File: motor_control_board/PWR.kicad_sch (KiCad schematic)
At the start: 16 parts

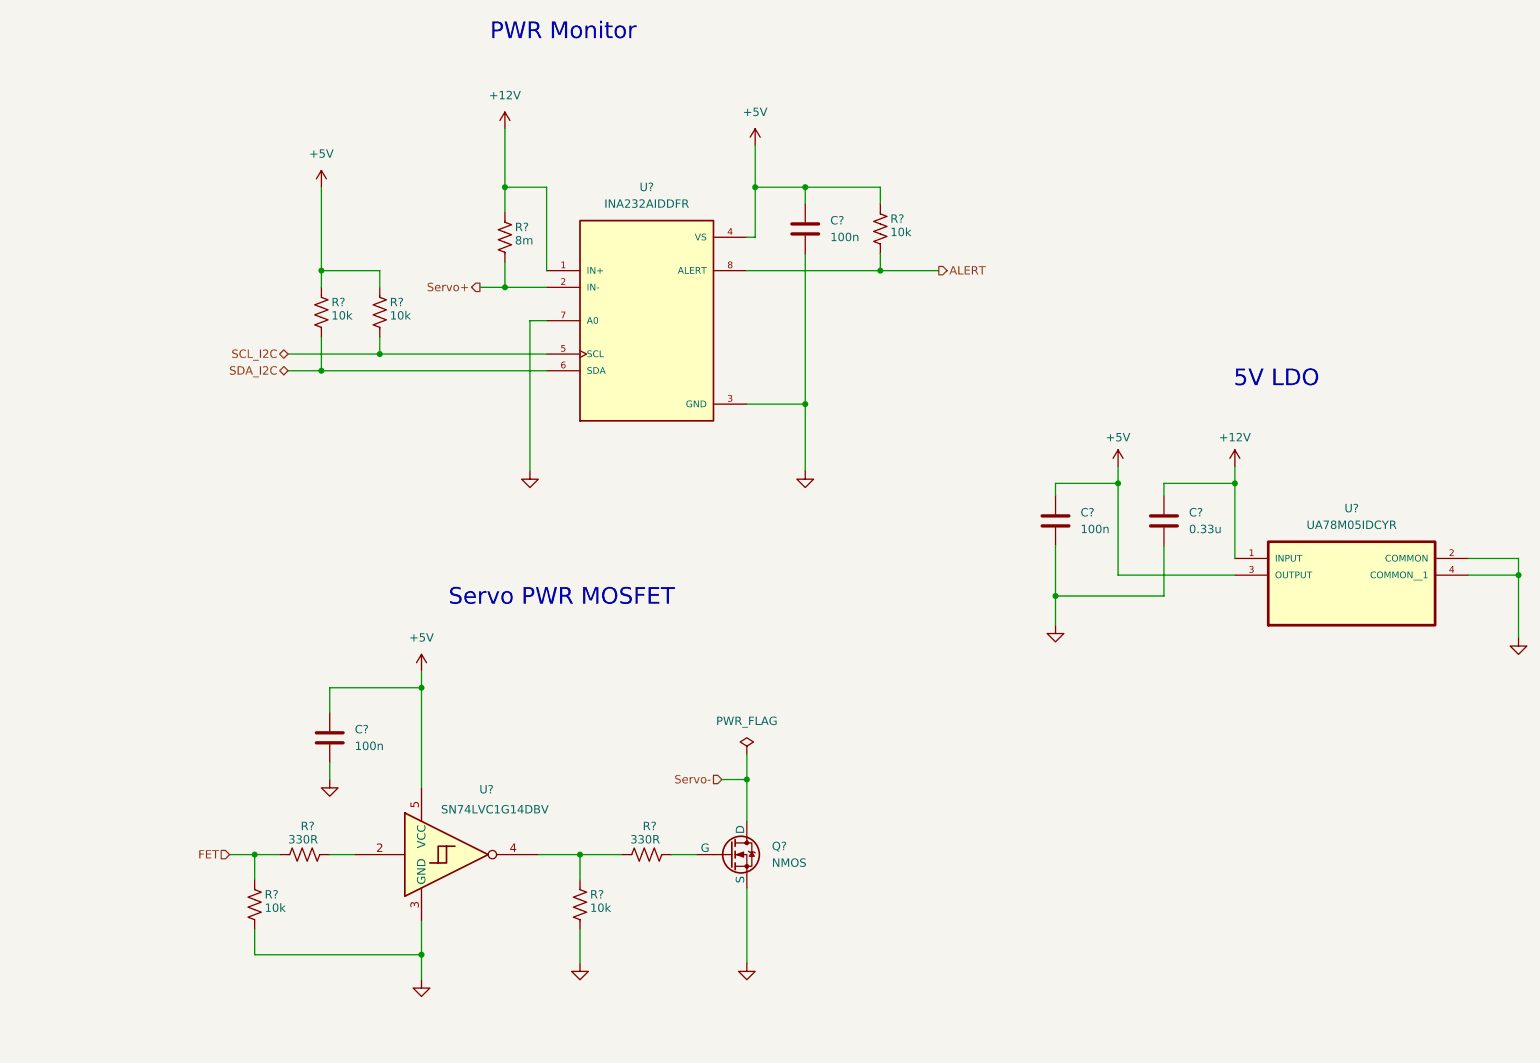
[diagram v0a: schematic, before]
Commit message: Minor schematic edits
Annotated schematic, selected mosfet and diodes, addressed comments
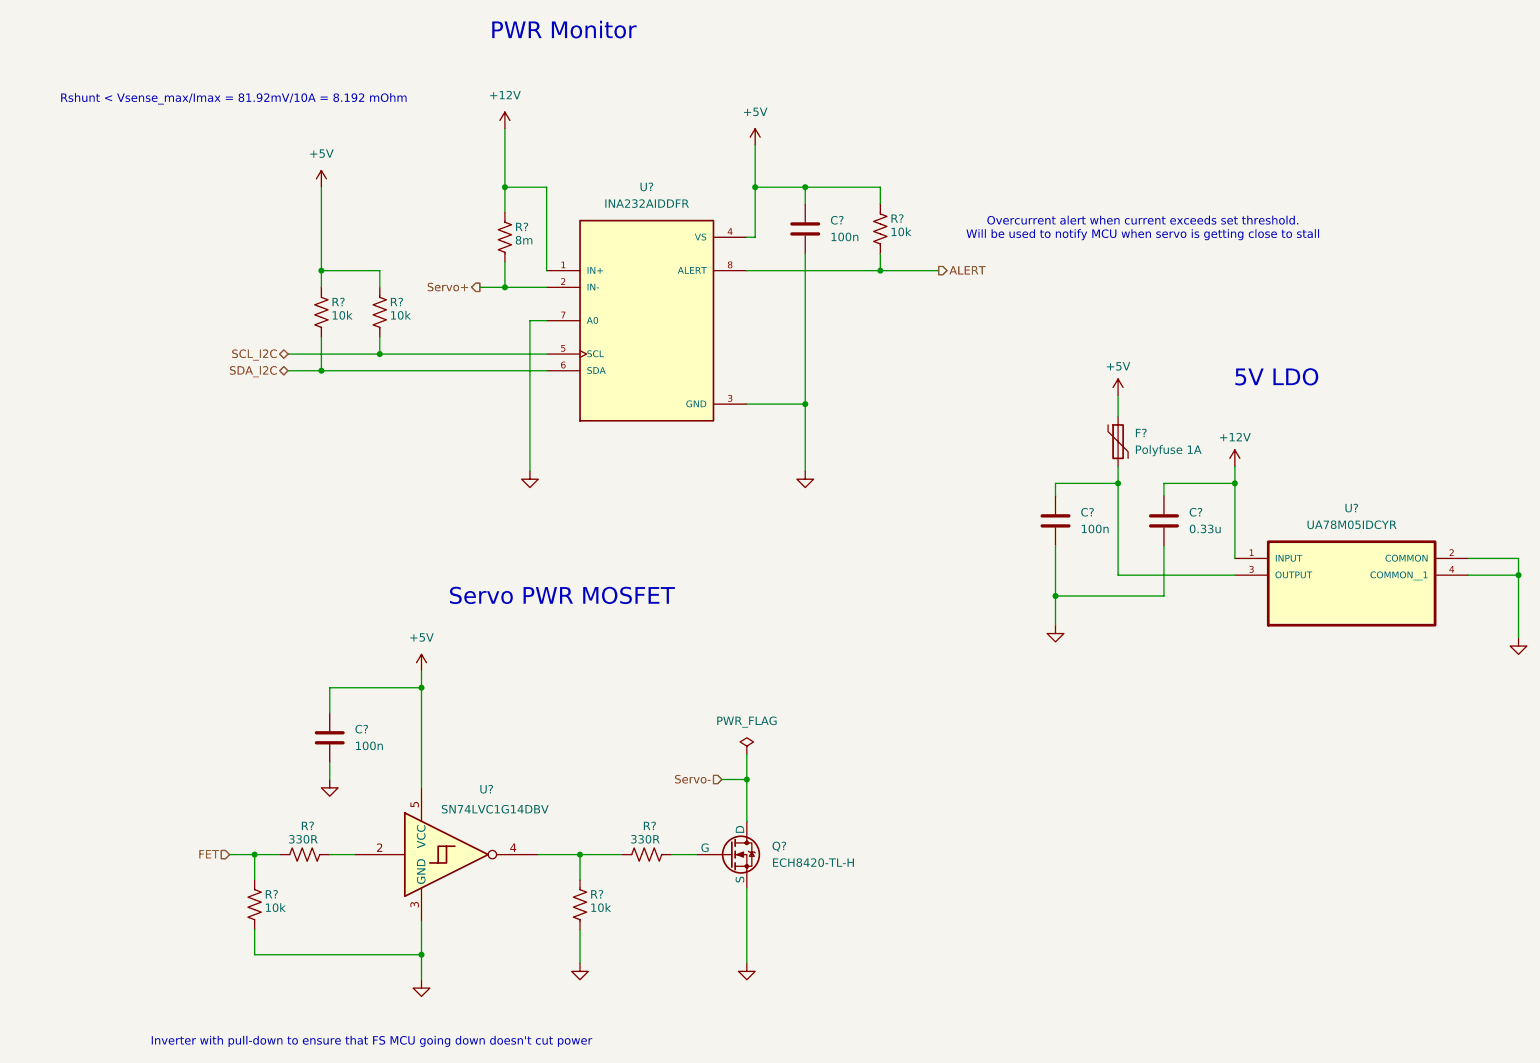
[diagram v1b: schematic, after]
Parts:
- added F?: Polyfuse 1A, symbol canhw:Polyfuse
- Q?: value NMOS -> ECH8420-TL-H
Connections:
- net +5V: now also F?.1; no longer C?.1, U?.3 (OUTPUT)
- new net: C?.1, F?.2, U?.3 (OUTPUT)
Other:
- note added: "Inverter with pull-down to ensure that FS MCU going down doesn't cut power"
- note added: "Overcurrent alert when current exceeds set threshold. Will be used to notify MCU when servo is getting close to stall"
- note added: "Rshunt < Vsense_max/Imax = 81.92mV/10A = 8.192 mOhm"
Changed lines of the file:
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@@
+	(wire
+		(pts
+			(xy 200.025 87.63) (xy 200.025 90.805)
+		)
+		(stroke
+			(width 0)
+			(type default)
+		)
+	)
 	(wire
 		(pts
@@
 		)
 	)
+	(text "Inverter with pull-down to ensure that FS MCU going down doesn't cut power"
+		(exclude_from_sim no)
+		(at 86.36 186.055 0)
+		(effects
+			(font
+				(size 1.27 1.27)
+			)
+		)
+	)
 	(text "5V LDO"
 		(exclude_from_sim no)
@@
 		)
 	)
+	(text "Overcurrent alert when current exceeds set threshold.\nWill be used to notify MCU when servo is getting close to stall"
+		(exclude_from_sim no)
+		(at 203.835 62.23 0)
+		(effects
+			(font
+				(size 1.27 1.27)
+			)
+		)
+	)
+	(text "Rshunt < Vsense_max/Imax = 81.92mV/10A = 8.192 mOhm"
+		(exclude_from_sim no)
+		(at 65.405 42.545 0)
+		(effects
+			(font
+				(size 1.27 1.27)
+			)
+		)
+	)
 	(hierarchical_label "SCL_I2C"
 		(shape bidirectional)
@@
 	(symbol
 		(lib_id "canhw:+5V")
-		(at 200.025 98.425 0)
+		(at 200.025 87.63 0)
 		(unit 1)
 		(exclude_from_sim no)
@@
 		(fields_autoplaced yes)
 		(property "Reference" "#PWR028"
-			(at 200.025 102.235 0)
+			(at 200.025 91.44 0)
 			(effects
 				(font
@@
 		)
 		(property "Value" "+5V"
-			(at 200.025 93.98 0)
+			(at 200.025 83.185 0)
 			(effects
 				(font
@@
 		)
 		(property "Footprint" ""
-			(at 200.025 98.425 0)
+			(at 200.025 87.63 0)
 			(effects
 				(font
@@
 		)
 		(property "Datasheet" ""
-			(at 200.025 98.425 0)
+			(at 200.025 87.63 0)
 			(effects
 				(font
@@
 		)
 		(property "Description" "Power symbol creates a global label with name \"+5V\""
-			(at 200.025 98.425 0)
+			(at 200.025 87.63 0)
 			(effects
 				(font
@@
 			)
 		)
-		(property "Value" "NMOS"
+		(property "Value" "ECH8420-TL-H"
 			(at 147.32 158.7499 0)
 			(effects
@@
 			)
 		)
-		(property "Datasheet" "https://ngspice.sourceforge.io/docs/ngspice-html-manual/manual.xhtml#cha_MOSFETs"
+		(property "Datasheet" "https://www.onsemi.com/download/data-sheet/pdf/ech8420-d.pdf"
 			(at 140.97 170.18 0)
 			(effects
@@
 			)
 		)
+		(property "Purpose" ""
+			(at 140.97 157.48 0)
+			(effects
+				(font
+					(size 1.27 1.27)
+				)
+			)
+		)
 		(pin "2"
 		)
@@
 					(unit 1)
 				)
+			)
+		)
+	)
+	(symbol
+		(lib_id "canhw:Polyfuse")
+		(at 200.025 94.615 0)
+		(unit 1)
+		(exclude_from_sim no)
+		(in_bom yes)
+		(on_board yes)
+		(dnp no)
+		(property "Reference" "F?"
+			(at 202.565 93.345 0)
+			(effects
+				(font
+					(size 1.27 1.27)
+				)
+				(justify left)
+			)
+		)
+		(property "Value" "Polyfuse 1A"
+			(at 202.565 95.885 0)
+			(effects
+				(font
+					(size 1.27 1.27)
+				)
+				(justify left)
+			)
+		)
+		(property "Footprint" ""
+			(at 201.295 99.695 0)
+			(effects
+				(font
+					(size 1.27 1.27)
+				)
+				(justify left)
+				(hide yes)
+			)
+		)
+		(property "Datasheet" "~"
+			(at 200.025 94.615 0)
+			(effects
+				(font
+					(size 1.27 1.27)
+				)
+				(hide yes)
+			)
+		)
+		(property "Description" "Resettable fuse, polymeric positive temperature coefficient"
+			(at 200.025 94.615 0)
+			(effects
+				(font
+					(size 1.27 1.27)
+				)
+				(hide yes)
+			)
+		)
+		(pin "2"
+		)
+		(pin "1"
+		)
+		(instances
+			(project "motor_control_board"
+				(path "/ced26b11-410b-4897-bfe1-68b095b3fef4/6d921c46-a69c-4b88-8fde-0dba583b7bde"
+					(reference "F?")
+					(unit 1)
+				)

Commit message: Added second encoder connection, minor edits
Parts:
- R22: renamed from R?; value 8m -> 13m
- gave numbers to parts that had none: 16
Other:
- note added: "Rshunt < Vsense_max/Imax = 81.92mV/5A = 16.384 mOhm"
- note removed: "Rshunt < Vsense_max/Imax = 81.92mV/10A = 8.192 mOhm"
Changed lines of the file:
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@@
 	)
 	(junction
-		(at 190.5 118.11)
-		(diameter 0)
-		(color 0 0 0 0)
-	)
-	(junction
 		(at 78.74 68.58)
 		(diameter 0)
@@
 	(wire
 		(pts
-			(xy 190.5 110.49) (xy 190.5 118.11)
-		)
-		(stroke
-			(width 0)
-			(type default)
-		)
-	)
-	(wire
-		(pts
 			(xy 152.4 55.88) (xy 144.78 55.88)
 		)
@@
 	(wire
 		(pts
-			(xy 190.5 118.11) (xy 190.5 122.555)
+			(xy 190.5 110.49) (xy 190.5 118.11)
 		)
 		(stroke
@@
 	(wire
 		(pts
-			(xy 207.01 118.11) (xy 190.5 118.11)
-		)
-		(stroke
-			(width 0)
-			(type default)
-		)
-	)
-	(wire
-		(pts
 			(xy 87.63 78.74) (xy 87.63 81.28)
 		)
@@
 		)
 	)
-	(text "Rshunt < Vsense_max/Imax = 81.92mV/10A = 8.192 mOhm"
+	(text "Rshunt < Vsense_max/Imax = 81.92mV/5A = 16.384 mOhm"
 		(exclude_from_sim no)
 		(at 65.405 42.545 0)
@@
 		(dnp no)
 		(fields_autoplaced yes)
-		(property "Reference" "C?"
+		(property "Reference" "C13"
 			(at 156.21 60.9599 0)
 			(effects
@@
 			(project "Motor Control Board"
 				(path "/ced26b11-410b-4897-bfe1-68b095b3fef4/6d921c46-a69c-4b88-8fde-0dba583b7bde"
-					(reference "C?")
+					(reference "C13")
 					(unit 1)
 				)
@@
 		(on_board yes)
 		(dnp no)
-		(property "Reference" "R?"
+		(property "Reference" "R22"
 			(at 108.204 61.976 0)
 			(effects
@@
 			)
 		)
-		(property "Value" "8m"
+		(property "Value" "13m"
 			(at 108.204 64.008 0)
 			(effects
@@
 			(project "Motor Control Board"
 				(path "/ced26b11-410b-4897-bfe1-68b095b3fef4/6d921c46-a69c-4b88-8fde-0dba583b7bde"
-					(reference "R?")
+					(reference "R22")
 					(unit 1)
 				)
@@
 	(symbol
 		(lib_id "canhw:GND")
-		(at 190.5 122.555 0)
+		(at 190.5 118.11 0)
 		(unit 1)
 		(exclude_from_sim no)
@@
 		(fields_autoplaced yes)
 		(property "Reference" "#PWR038"
-			(at 190.5 128.905 0)
+			(at 190.5 124.46 0)
 			(effects
 				(font
@@
 		)
 		(property "Value" "GND"
-			(at 190.5 127.635 0)
+			(at 190.5 123.19 0)
 			(effects
 				(font
@@
 		)
 		(property "Footprint" ""
-			(at 190.5 122.555 0)
+			(at 190.5 118.11 0)
 			(effects
 				(font
@@
 		)
 		(property "Datasheet" ""
-			(at 190.5 122.555 0)
+			(at 190.5 118.11 0)
 			(effects
 				(font
@@
 		)
 		(property "Description" "Power symbol creates a global label with name \"GND\" , ground"
-			(at 190.5 122.555 0)
+			(at 190.5 118.11 0)
 			(effects
 				(font
@@
 		)
 		(property "Purpose" ""
-			(at 190.5 122.555 0)
+			(at 190.5 118.11 0)
 			(effects
 				(font
@@
 		(dnp no)
 		(fields_autoplaced yes)
-		(property "Reference" "U?"
+		(property "Reference" "U8"
 			(at 235.585 104.775 0)
 			(effects
@@
 			(project ""
 				(path "/ced26b11-410b-4897-bfe1-68b095b3fef4/6d921c46-a69c-4b88-8fde-0dba583b7bde"
-					(reference "U?")
+					(reference "U8")
 					(unit 1)
 				)
@@
 		(on_board yes)
 		(dnp no)
-		(property "Reference" "R?"
+		(property "Reference" "R19"
 			(at 77.724 153.162 90)
 			(effects
@@
 			(project "Motor Control Board"
 				(path "/ced26b11-410b-4897-bfe1-68b095b3fef4/6d921c46-a69c-4b88-8fde-0dba583b7bde"
-					(reference "R?")
+					(reference "R19")
 					(unit 1)
 				)
@@
 		(dnp no)
 		(fields_autoplaced yes)
-		(property "Reference" "C?"
+		(property "Reference" "C12"
 			(at 83.82 138.4299 0)
 			(effects
@@
 			(project "Motor Control Board"
 				(path "/ced26b11-410b-4897-bfe1-68b095b3fef4/6d921c46-a69c-4b88-8fde-0dba583b7bde"
-					(reference "C?")
+					(reference "C12")
 					(unit 1)
 				)
@@
 		(on_board yes)
 		(dnp no)
-		(property "Reference" "R?"
+		(property "Reference" "R18"
 			(at 70.104 163.576 0)
 			(effects
@@
 			(project "Motor Control Board"
 				(path "/ced26b11-410b-4897-bfe1-68b095b3fef4/6d921c46-a69c-4b88-8fde-0dba583b7bde"
-					(reference "R?")
+					(reference "R18")
 					(unit 1)
 				)
@@
 		(dnp no)
 		(fields_autoplaced yes)
-		(property "Reference" "Q?"
+		(property "Reference" "Q1"
 			(at 147.32 156.2099 0)
 			(effects
@@
 			(project "Motor Control Board"
 				(path "/ced26b11-410b-4897-bfe1-68b095b3fef4/6d921c46-a69c-4b88-8fde-0dba583b7bde"
-					(reference "Q?")
+					(reference "Q1")
 					(unit 1)
 				)
@@
 		(dnp no)
 		(fields_autoplaced yes)
-		(property "Reference" "U?"
+		(property "Reference" "U7"
 			(at 128.27 55.88 0)
 			(effects
@@
 			(project "Motor Control Board"
 				(path "/ced26b11-410b-4897-bfe1-68b095b3fef4/6d921c46-a69c-4b88-8fde-0dba583b7bde"
-					(reference "U?")
+					(reference "U7")
 					(unit 1)
 				)
@@
 		(on_board yes)
 		(dnp no)
-		(property "Reference" "U?"
+		(property "Reference" "U6"
 			(at 103.886 147.574 0)
 			(effects
@@
 			(project ""
 				(path "/ced26b11-410b-4897-bfe1-68b095b3fef4/6d921c46-a69c-4b88-8fde-0dba583b7bde"
-					(reference "U?")
+					(reference "U6")
 					(unit 1)
 				)
@@
 		(on_board yes)
 		(dnp no)
-		(property "Reference" "R?"
+		(property "Reference" "R21"
 			(at 89.154 73.406 0)
 			(effects
@@
 			(project "Motor Control Board"
 				(path "/ced26b11-410b-4897-bfe1-68b095b3fef4/6d921c46-a69c-4b88-8fde-0dba583b7bde"
-					(reference "R?")
+					(reference "R21")
 					(unit 1)
 				)
@@
 		(on_board yes)
 		(dnp no)
-		(property "Reference" "R?"
+		(property "Reference" "R25"
 			(at 165.354 60.706 0)
 			(effects
@@
 			(project "Motor Control Board"
 				(path "/ced26b11-410b-4897-bfe1-68b095b3fef4/6d921c46-a69c-4b88-8fde-0dba583b7bde"
-					(reference "R?")
+					(reference "R25")
 					(unit 1)
 				)
@@
 		(on_board yes)
 		(dnp no)
-		(property "Reference" "F?"
+		(property "Reference" "F3"
 			(at 202.565 93.345 0)
 			(effects
@@
 			(project "motor_control_board"
 				(path "/ced26b11-410b-4897-bfe1-68b095b3fef4/6d921c46-a69c-4b88-8fde-0dba583b7bde"
-					(reference "F?")
+					(reference "F3")
 					(unit 1)
 				)
@@
 		(on_board yes)
 		(dnp no)
-		(property "Reference" "R?"
+		(property "Reference" "R23"
 			(at 119.634 163.576 0)
 			(effects
@@
 			(project "Motor Control Board"
 				(path "/ced26b11-410b-4897-bfe1-68b095b3fef4/6d921c46-a69c-4b88-8fde-0dba583b7bde"
-					(reference "R?")
+					(reference "R23")
+					(unit 1)
+				)
+			)
+		)
+	)
+	(symbol
+		(lib_id "canhw:GND")
+		(at 207.01 118.11 0)
+		(unit 1)
+		(exclude_from_sim no)
+		(in_bom yes)
+		(on_board yes)
+		(dnp no)
+		(fields_autoplaced yes)
+		(property "Reference" "#PWR046"
+			(at 207.01 124.46 0)
+			(effects
+				(font
+					(size 1.27 1.27)
+				)
+				(hide yes)
+			)
+		)
+		(property "Value" "GND"
+			(at 207.01 123.19 0)
+			(effects
+				(font
+					(size 1.27 1.27)
+				)
+				(hide yes)
+			)
+		)
+		(property "Footprint" ""
+			(at 207.01 118.11 0)
+			(effects
+				(font
+					(size 1.27 1.27)
+				)
+				(hide yes)
+			)
+		)
+		(property "Datasheet" ""
+			(at 207.01 118.11 0)
+			(effects
+				(font
+					(size 1.27 1.27)
+				)
+				(hide yes)
+			)
+		)
+		(property "Description" "Power symbol creates a global label with name \"GND\" , ground"
+			(at 207.01 118.11 0)
+			(effects
+				(font
+					(size 1.27 1.27)
+				)
+				(hide yes)
+			)
+		)
+		(property "Purpose" ""
+			(at 207.01 118.11 0)
+			(effects
+				(font
+					(size 1.27 1.27)
+				)
+			)
+		)
+		(pin "1"
+		)
+		(instances
+			(project "motor_control_board"
+				(path "/ced26b11-410b-4897-bfe1-68b095b3fef4/6d921c46-a69c-4b88-8fde-0dba583b7bde"
+					(reference "#PWR046")
 					(unit 1)
 				)
@@
 		(dnp no)
 		(fields_autoplaced yes)
-		(property "Reference" "C?"
+		(property "Reference" "C15"
 			(at 210.82 105.4099 0)
 			(effects
@@
 			(project ""
 				(path "/ced26b11-410b-4897-bfe1-68b095b3fef4/6d921c46-a69c-4b88-8fde-0dba583b7bde"
-					(reference "C?")
+					(reference "C15")
 					(unit 1)
 				)
@@
 		(dnp no)
 		(fields_autoplaced yes)
-		(property "Reference" "C?"
+		(property "Reference" "C14"
 			(at 194.31 105.4099 0)
 			(effects
@@
 			(project "Motor Control Board"
 				(path "/ced26b11-410b-4897-bfe1-68b095b3fef4/6d921c46-a69c-4b88-8fde-0dba583b7bde"
-					(reference "C?")
+					(reference "C14")
 					(unit 1)
 				)
@@
 		(on_board yes)
 		(dnp no)
-		(property "Reference" "R?"
+		(property "Reference" "R20"
 			(at 80.264 73.406 0)
 			(effects
@@
 			(project "Motor Control Board"
 				(path "/ced26b11-410b-4897-bfe1-68b095b3fef4/6d921c46-a69c-4b88-8fde-0dba583b7bde"
-					(reference "R?")
+					(reference "R20")
 					(unit 1)
 				)
@@
 		(on_board yes)
 		(dnp no)
-		(property "Reference" "R?"
+		(property "Reference" "R24"
 			(at 129.794 153.162 90)
 			(effects
@@
 			(project "Motor Control Board"
 				(path "/ced26b11-410b-4897-bfe1-68b095b3fef4/6d921c46-a69c-4b88-8fde-0dba583b7bde"
-					(reference "R?")
+					(reference "R24")
 					(unit 1)
 				)

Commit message: assigned footprints
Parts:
- C12, C13: footprint Capacitor_SMD:C_0402_1005Metric -> Capacitor_SMD:C_0805_2012Metric_Pad1.18x1.45mm_HandSolder
- C14, C15: footprint (none) -> Capacitor_SMD:C_0805_2012Metric_Pad1.18x1.45mm_HandSolder
- F3: footprint (none) -> Fuse:Fuse_1206_3216Metric_Pad1.42x1.75mm_HandSolder
- Q1: footprint (none) -> Package_TO_SOT_SMD:OnSemi_ECH8
- R18, R19, R20, R21, R23, R24, R25: footprint (none) -> Resistor_SMD:R_0805_2012Metric_Pad1.20x1.40mm_HandSolder
- R22: footprint (none) -> Resistor_SMD:R_1206_3216Metric_Pad1.30x1.75mm_HandSolder
- U7: footprint INA232AIDDFR:SOT65P280X110-8N -> motor-control:SOT65P280X110-8N
- U8: footprint UA78M05IDCYR:SOT230P700X180-4N -> motor-control:SOT230P700X180-4N
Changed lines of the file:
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@@
 			)
 		)
-		(property "Footprint" "Capacitor_SMD:C_0402_1005Metric"
+		(property "Footprint" "Capacitor_SMD:C_0805_2012Metric_Pad1.18x1.45mm_HandSolder"
 			(at 153.3652 66.04 0)
 			(effects
@@
 			)
 		)
-		(property "Footprint" ""
+		(property "Footprint" "Resistor_SMD:R_1206_3216Metric_Pad1.30x1.75mm_HandSolder"
 			(at 107.696 63.754 90)
 			(effects
@@
 			)
 		)
-		(property "Footprint" "UA78M05IDCYR:SOT230P700X180-4N"
+		(property "Footprint" "motor-control:SOT230P700X180-4N"
 			(at 235.585 114.935 0)
 			(effects
@@
 			)
 		)
-		(property "Footprint" ""
+		(property "Footprint" "Resistor_SMD:R_0805_2012Metric_Pad1.20x1.40mm_HandSolder"
 			(at 76.454 156.464 90)
 			(effects
@@
 			)
 		)
-		(property "Footprint" "Capacitor_SMD:C_0402_1005Metric"
+		(property "Footprint" "Capacitor_SMD:C_0805_2012Metric_Pad1.18x1.45mm_HandSolder"
 			(at 80.9752 143.51 0)
 			(effects
@@
 			)
 		)
-		(property "Footprint" ""
+		(property "Footprint" "Resistor_SMD:R_0805_2012Metric_Pad1.20x1.40mm_HandSolder"
 			(at 69.596 165.354 90)
 			(effects
@@
 			)
 		)
-		(property "Footprint" ""
+		(property "Footprint" "Package_TO_SOT_SMD:OnSemi_ECH8"
 			(at 146.05 154.94 0)
 			(effects
@@
 			)
 		)
-		(property "Footprint" "INA232AIDDFR:SOT65P280X110-8N"
+		(property "Footprint" "motor-control:SOT65P280X110-8N"
 			(at 128.27 76.2 0)
 			(effects
@@
 			)
 		)
-		(property "Footprint" ""
+		(property "Footprint" "Resistor_SMD:R_0805_2012Metric_Pad1.20x1.40mm_HandSolder"
 			(at 88.646 75.184 90)
 			(effects
@@
 			)
 		)
-		(property "Footprint" ""
+		(property "Footprint" "Resistor_SMD:R_0805_2012Metric_Pad1.20x1.40mm_HandSolder"
 			(at 164.846 62.484 90)
 			(effects
@@
 			)
 		)
-		(property "Footprint" ""
+		(property "Footprint" "Fuse:Fuse_1206_3216Metric_Pad1.42x1.75mm_HandSolder"
 			(at 201.295 99.695 0)
 			(effects
@@
 			)
 		)
-		(property "Footprint" ""
+		(property "Footprint" "Resistor_SMD:R_0805_2012Metric_Pad1.20x1.40mm_HandSolder"
 			(at 119.126 165.354 90)
 			(effects
@@
 			)
 		)
-		(property "Footprint" ""
+		(property "Footprint" "Capacitor_SMD:C_0805_2012Metric_Pad1.18x1.45mm_HandSolder"
 			(at 207.9752 110.49 0)
 			(effects
@@
 			)
 		)
-		(property "Footprint" ""
+		(property "Footprint" "Capacitor_SMD:C_0805_2012Metric_Pad1.18x1.45mm_HandSolder"
 			(at 191.4652 110.49 0)
 			(effects
@@
 			)
 		)
-		(property "Footprint" ""
+		(property "Footprint" "Resistor_SMD:R_0805_2012Metric_Pad1.20x1.40mm_HandSolder"
 			(at 79.756 75.184 90)
 			(effects
@@
 			)
 		)
-		(property "Footprint" ""
+		(property "Footprint" "Resistor_SMD:R_0805_2012Metric_Pad1.20x1.40mm_HandSolder"
 			(at 128.524 156.464 90)
 			(effects
